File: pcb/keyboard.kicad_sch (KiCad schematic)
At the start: 28 parts, among them J1 Conn_ARM_JTAG_SWD_10, J3 Conn_Coaxial, SW1 SW_SPST, U1 nRF52840, X1 32MHz

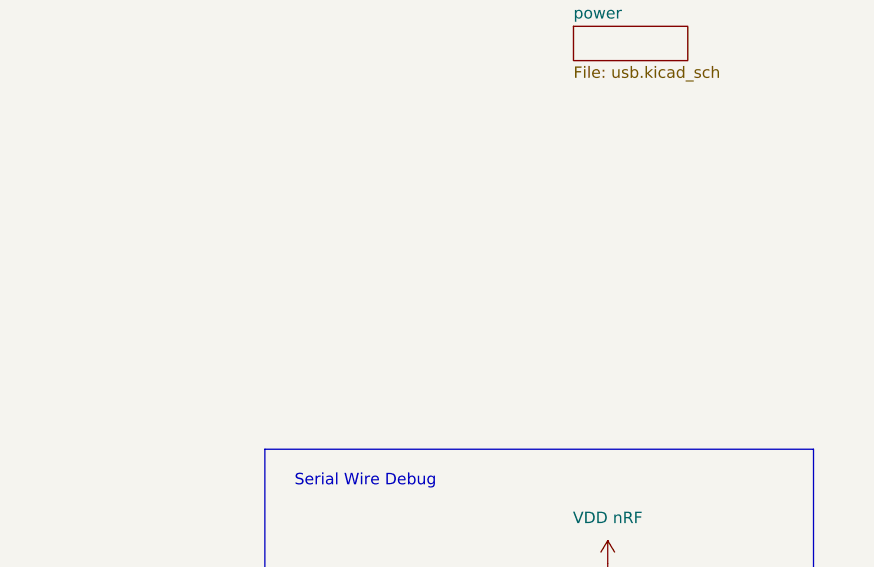
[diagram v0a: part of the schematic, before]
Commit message: Add mounting points
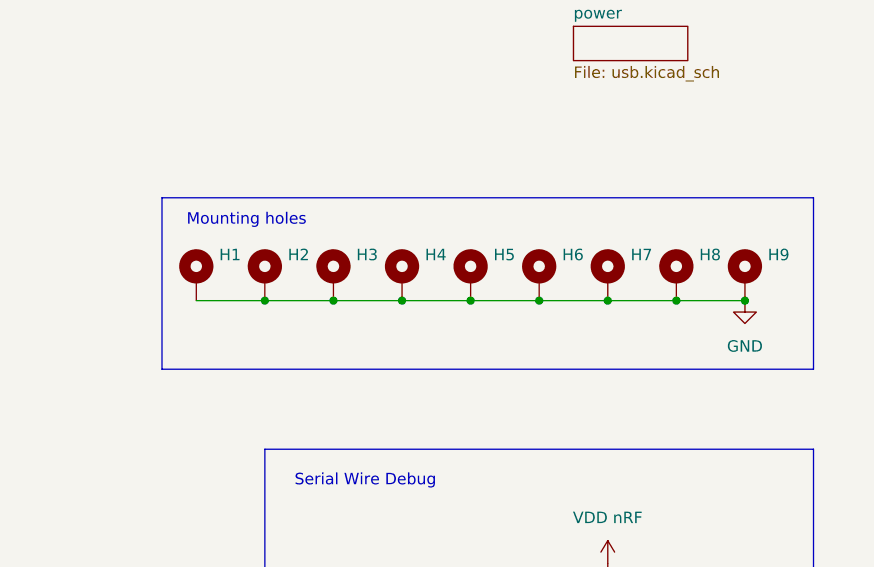
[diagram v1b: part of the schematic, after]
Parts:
- added H1, H2, H3, H4, H5, H6, H7, H8, H9: MountingHole_Pad, MountingHole:MountingHole_2.2mm_M2_Pad_Via, symbol Mechanical:MountingHole_Pad
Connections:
- net GND: now also H1.1, H2.1, H3.1, H4.1, H5.1, H6.1, H7.1, H8.1, H9.1
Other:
- note added: "Mounting holes"

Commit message: Add final hand solder footprints
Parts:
- J3: footprint Connector_Coaxial:SMA_Molex_73251-1153_EdgeMount_Horizontal -> My_Footprints:SMA_Molex_73251-1153_EdgeMount_Horizontal_HandSolder
- X1: footprint Crystal:Crystal_SMD_2016-4Pin_2.0x1.6mm -> My_Footprints:Crystal_SMD_2016-4Pin_2.0x1.6mm_HandSolder
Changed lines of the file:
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@@
 			)
 		)
-		(property "Footprint" "Connector_Coaxial:SMA_Molex_73251-1153_EdgeMount_Horizontal"
+		(property "Footprint" "My_Footprints:SMA_Molex_73251-1153_EdgeMount_Horizontal_HandSolder"
 			(at 36.83 72.39 0)
 			(hide yes)
@@
 			)
 		)
-		(property "Footprint" "Crystal:Crystal_SMD_2016-4Pin_2.0x1.6mm"
+		(property "Footprint" "My_Footprints:Crystal_SMD_2016-4Pin_2.0x1.6mm_HandSolder"
 			(at 62.23 118.11 0)
 			(hide yes)

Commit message: In case I fuck it up
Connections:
- net col0: no longer U1.D2 (XL1/P0.00)
- net col1: no longer U1.F2 (XL2/P0.01)
- net col10: now also U1.U24 (P1.04); no longer U1.J24 (NFC2/P0.10)
- net col11: now also U1.R24 (P1.06); no longer U1.T2 (TRACEDATA2/P0.11)
- net col12: now also U1.N24 (DEC5); no longer U1.U1 (TRACEDATA1/P0.12)
- net col13: now also U1.L24 (NFC1/P0.09); no longer U1.AD8 (P0.13)
- net col14: now also U1.J24 (NFC2/P0.10); no longer U1.AC9 (P0.14)
- net col2: now also U1.AB2 (DCCH); no longer U1.A12 (AIN0/P0.02)
- net col3: now also U1.AD8 (P0.13); no longer U1.B13 (AIN1/P0.03)
- net col4: now also U1.AD10 (P0.15); no longer U1.J1 (AIN2/P0.04)
- net col5: now also U1.AD12 (P0.17); no longer U1.K2 (AIN3/P0.05)
- net col6: now also U1.AD16 (P0.20); no longer U1.L1 (P0.06)
- net col7: now also U1.AD18 (P0.22); no longer U1.M2 (TRACECLK/P0.07)
- net col8: now also U1.AD20 (P0.24); no longer U1.N1 (P0.08)
- net col9: now also U1.W24 (P1.02); no longer U1.L24 (NFC1/P0.09)
- net row0: no longer U1.AD16 (P0.20)
- net row1: no longer U1.AC15 (P0.19)
- net row2: no longer U1.AD12 (P0.17)
- net row3: no longer U1.AC11 (P0.16)
- net row4: no longer U1.AD10 (P0.15)
- no-connect marks 29 -> 36

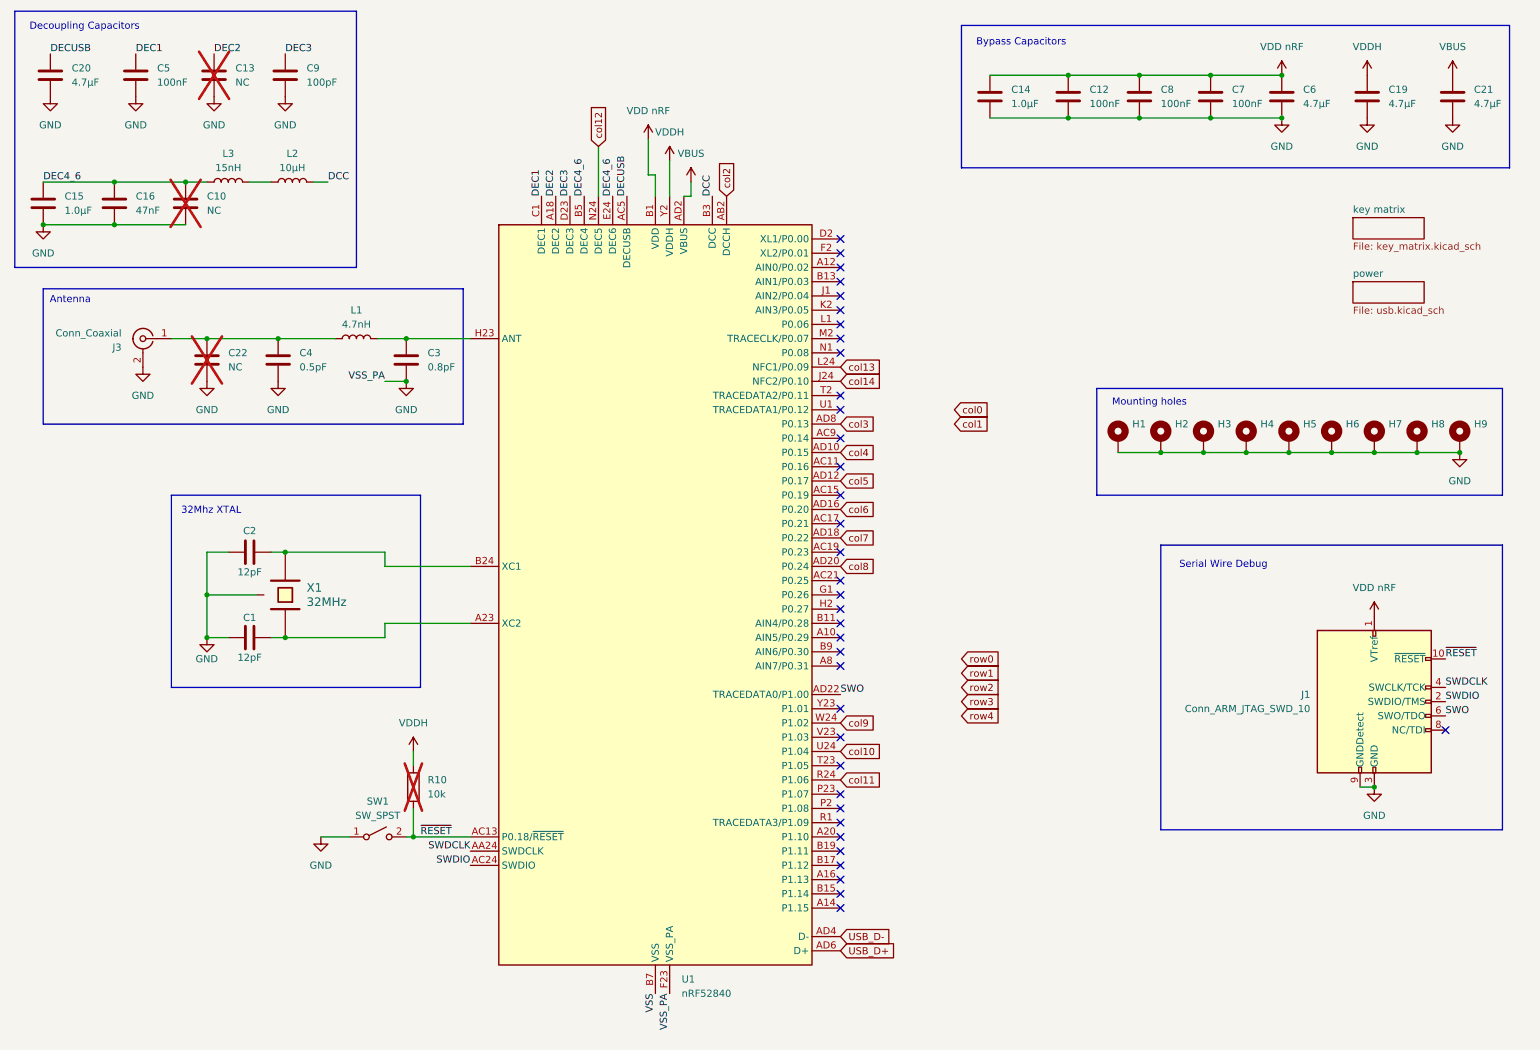
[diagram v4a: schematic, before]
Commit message: Finish initial routing
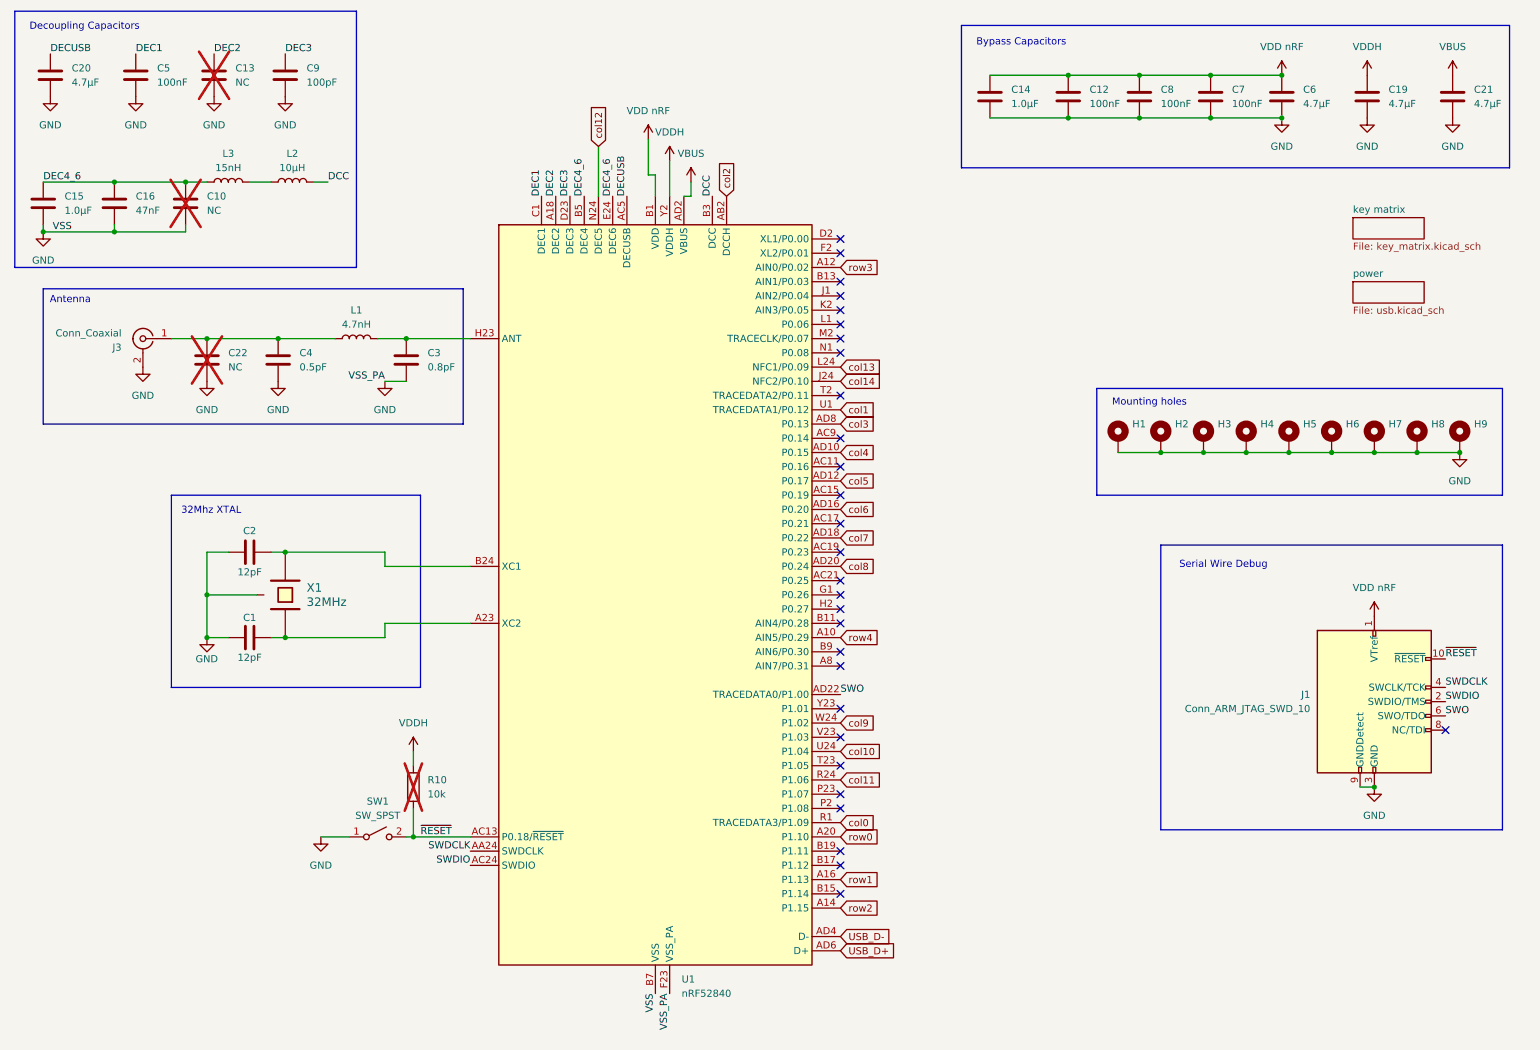
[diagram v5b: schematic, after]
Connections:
- net VSS is gone; now on net GND: U1.B7 (VSS), U1.EP (VSS)
- net col0: now also U1.R1 (TRACEDATA3/P1.09)
- net col1: now also U1.U1 (TRACEDATA1/P0.12)
- net row0: now also U1.A20 (P1.10)
- net row1: now also U1.A16 (P1.13)
- net row2: now also U1.A14 (P1.15)
- net row3: now also U1.A12 (AIN0/P0.02)
- net row4: now also U1.A10 (AIN5/P0.29)
- no-connect marks 36 -> 29
